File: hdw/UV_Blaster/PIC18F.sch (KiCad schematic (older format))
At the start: 14 parts

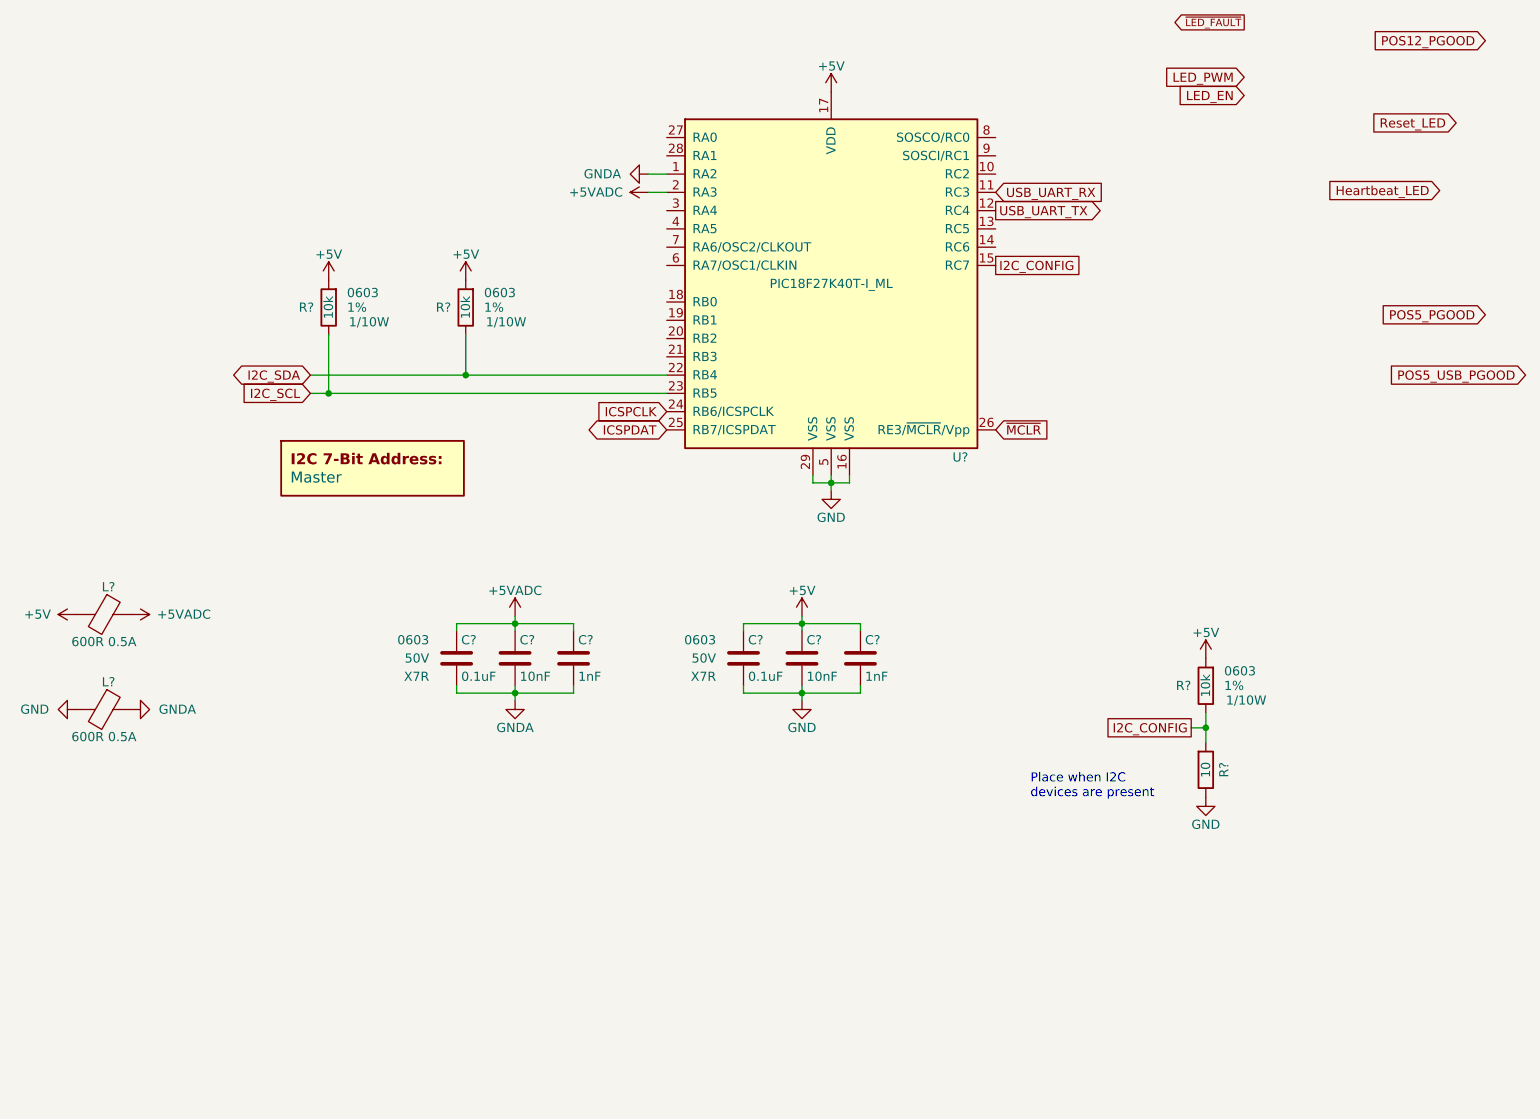
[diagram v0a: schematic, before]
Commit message: More sch work, netlist, part numbers, footprints
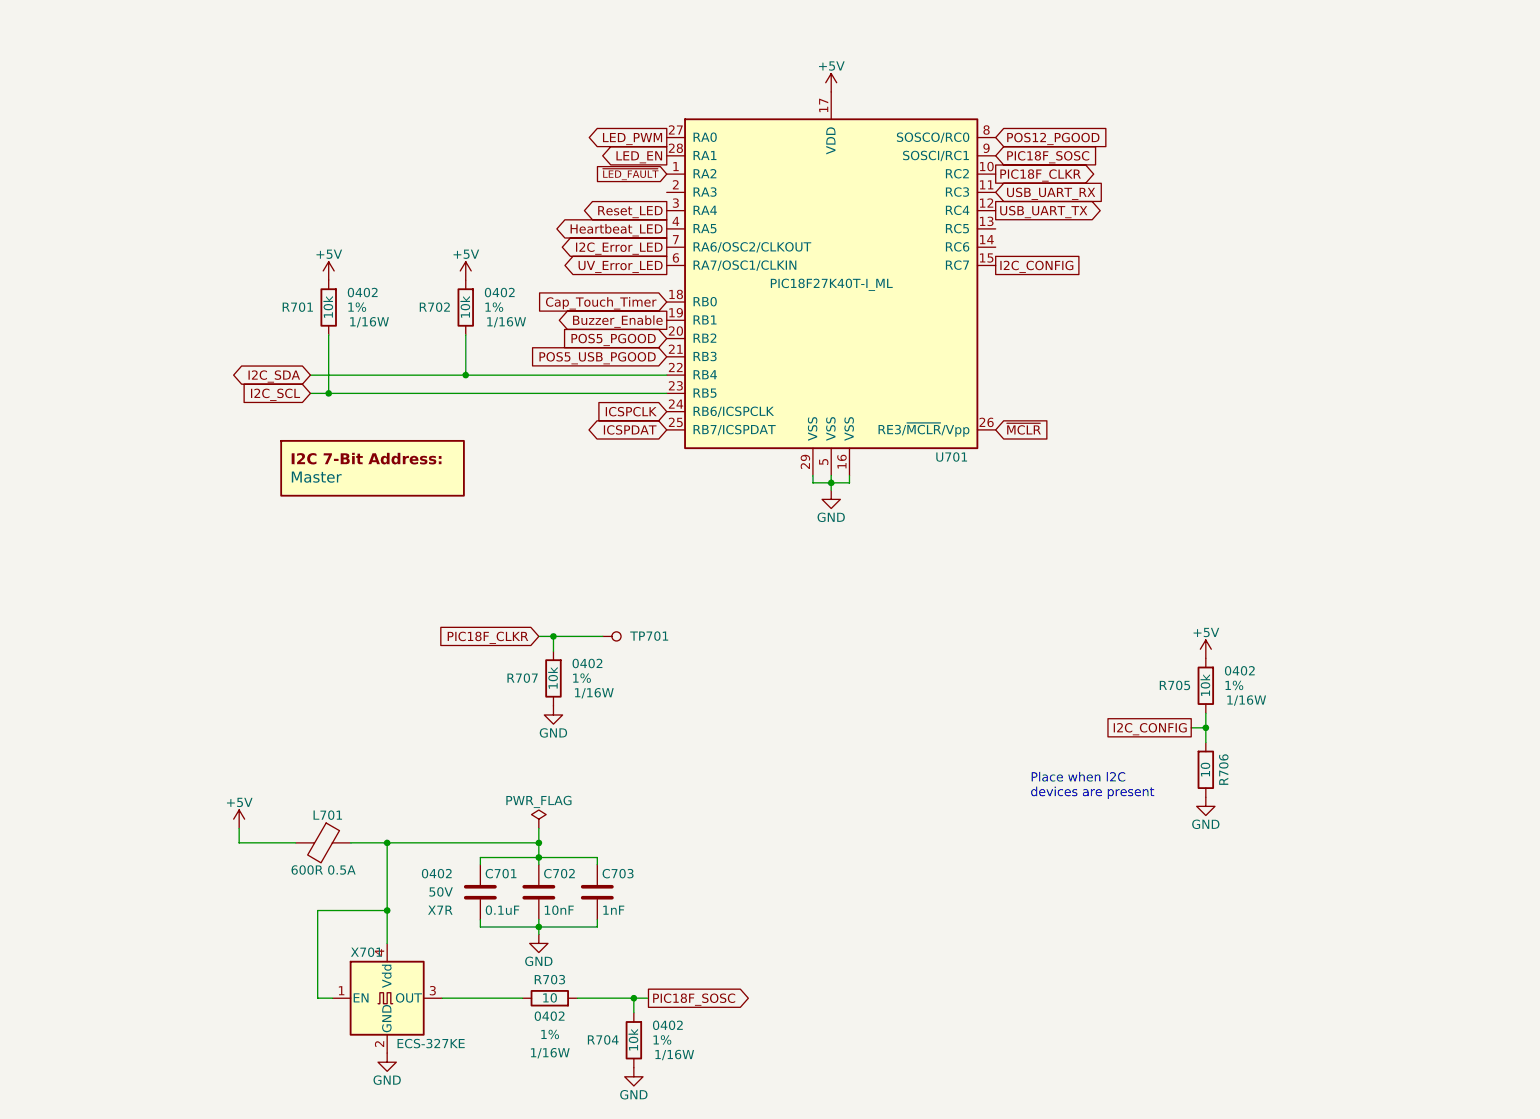
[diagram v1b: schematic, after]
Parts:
- removed C?: 0.1uF, Capacitors_SMD:C_0603, symbol Custom_Library:C_Custom
- removed C?: 10nF, Capacitors_SMD:C_0603, symbol Custom_Library:C_Custom
- removed C?: 1nF, Capacitors_SMD:C_0603, symbol Custom_Library:C_Custom
- removed L? (x2): 600R 0.5A, Inductors_SMD:L_0603, symbol Device:Ferrite_Bead
- added L701: 600R 0.5A, Inductors_SMD:L_0402, symbol Device:Ferrite_Bead
- added R703: 10, Resistors_SMD:R_0402, symbol Custom_Library:R_Custom
- added R704, R707: 10k, Resistors_SMD:R_0402, symbol Custom_Library:R_Custom
- added TP701: TP, Custom Footprints Library:Test_Point, symbol Custom_Library:TP
- added X701: ECS-327KE, Custom Footprints Library:ECS-327KE, symbol Custom_Library:ECS-327KE
- C701: renamed from C?; footprint Capacitors_SMD:C_0603 -> Capacitors_SMD:C_0402; Digi-Key PN 311-1344-1-ND -> 490-10701-1-ND; display_footprint 0603 -> 0402
- C702: renamed from C?; footprint Capacitors_SMD:C_0603 -> Capacitors_SMD:C_0402; Digi-Key PN 1276-1921-1-ND -> 490-13295-1-ND; display_footprint 0603 -> 0402
- C703: renamed from C?; footprint Capacitors_SMD:C_0603 -> Capacitors_SMD:C_0402; Digi-Key PN 1276-1018-1-ND -> 399-1032-1-ND; display_footprint 0603 -> 0402
- R701, R702, R705: renamed from R?; footprint Resistors_SMD:R_0603 -> Resistors_SMD:R_0402; Digi-Key PN RHM10KADCT-ND -> 541-3959-1-ND; Wattage 1/10W -> 1/16W; display_footprint 0603 -> 0402
- R706: renamed from R?; Configuration (none) -> Telemetry; Digi-Key PN (none) -> 311-10.0LRCT-ND
- gave numbers to parts that had none: 2
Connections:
- net GNDA is gone; now on net ~LED_FAULT: U701.1 (RA2)
- net +5V: now also L701.2; no longer C701.1, C702.1, C703.1
- net GND: now also R704.2, R707.2, X701.2 (GND)
- net Heartbeat_LED: now also U701.4 (RA5)
- net LED_EN: now also U701.28 (RA1)
- net LED_PWM: now also U701.27 (RA0)
- net POS12_PGOOD: now also U701.8 (SOSCO/RC0)
- net POS5_PGOOD: now also U701.20 (RB2)
- net POS5_USB_PGOOD: now also U701.21 (RB3)
- net Reset_LED: now also U701.3 (RA4)
- net PIC18F_CLKR: now reaches U701.10 (RC2)
- net PIC18F_CLKR: now also R707.1, TP701.1 (TP)
- net Cap_Touch_Timer: now reaches U701.18 (RB0)
- net Buzzer_Enable: now reaches U701.19 (RB1)
- net UV_Error_LED: now reaches U701.6 (RA7/OSC1/CLKIN)
- net I2C_Error_LED: now reaches U701.7 (RA6/OSC2/CLKOUT)
- net PIC18F_SOSC: now reaches U701.9 (SOSCI/RC1)
- net PIC18F_SOSC: now also R703.1, R704.1
- net +5VADC: no longer names the net of U701.2 (RA3)
- new net: C701.1, C702.1, C703.1, L701.1, X701.1 (EN), X701.4 (Vdd)
- new net: R703.2, X701.3 (OUT)
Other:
- moved on the sheet: C701, C702, C703
